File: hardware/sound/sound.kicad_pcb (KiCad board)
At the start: 2 copper layers, 177.8 x 114.3 mm, 38 parts, among them J1 Conn_01x02, J2 AVR-ISP-6, J3 Conn_01x02, J4 Conn_01x02, J5 Conn_01x02, J6 Conn_01x04, T1 125BSE, U1 6CY7, U2 SN76489, U3 ATtiny84A-P, X1 CXO_DIP8

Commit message: working on placement
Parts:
- added C10: 0.1uF, Capacitor_THT:C_Disc_D3.4mm_W2.1mm_P2.50mm, F.Cu at (101.6, 69.2)
- added C11: 2.2uF, Capacitor_THT:C_Disc_D3.4mm_W2.1mm_P2.50mm, F.Cu at (101.0, 121.9)
- added C9: 0.1uF, Capacitor_THT:C_Disc_D3.4mm_W2.1mm_P2.50mm, F.Cu at (101.6, 93.3)
- C3: value C -> 33uF 400V
- C8: value C -> 0.1uF
- LS1: footprint Connector_PinHeader_2.54mm:PinHeader_1x02_P2.54mm_Vertical -> Connector_Phoenix_MC_HighVoltage:PhoenixContact_MCV_1,5_2-G-5.08_1x02_P5.08mm_Vertical
- R10: footprint Resistor_SMD:R_1206_3216Metric_Pad1.30x1.75mm_HandSolder -> Resistor_THT:R_Axial_DIN0204_L3.6mm_D1.6mm_P5.08mm_Horizontal
- moved J5 107.2 mm to (214.0, 112.4)
- moved R10 97.5 mm to (104.8, 54.6), turned to -90 degrees
- moved J2 92.9 mm to (117.5, 54.6), turned to -90 degrees
- moved RV1 88.0 mm to (179.7, 151.3)
- moved LS1 69.3 mm to (150.5, 50.2)
- moved U3 54.8 mm to (106.0, 74.3), turned to 90 degrees
- moved R9 51.6 mm to (86.4, 126.4), turned to -90 degrees
- moved C2 49.0 mm to (212.9, 130.4), turned to 90 degrees
- moved U1 45.2 mm to (189.5, 131.2), turned to 90 degrees
- moved J3 43.2 mm to (87.6, 48.3), turned to 180 degrees
- moved R1 40.2 mm to (148.6, 151.9)
- moved C8 37.4 mm to (108.6, 123.8)
- moved D2 36.8 mm to (49.7, 99.2), turned to 90 degrees
- moved D1 35.9 mm to (49.7, 69.1), turned to -90 degrees
- moved R3 29.0 mm to (164.3, 112.8)
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
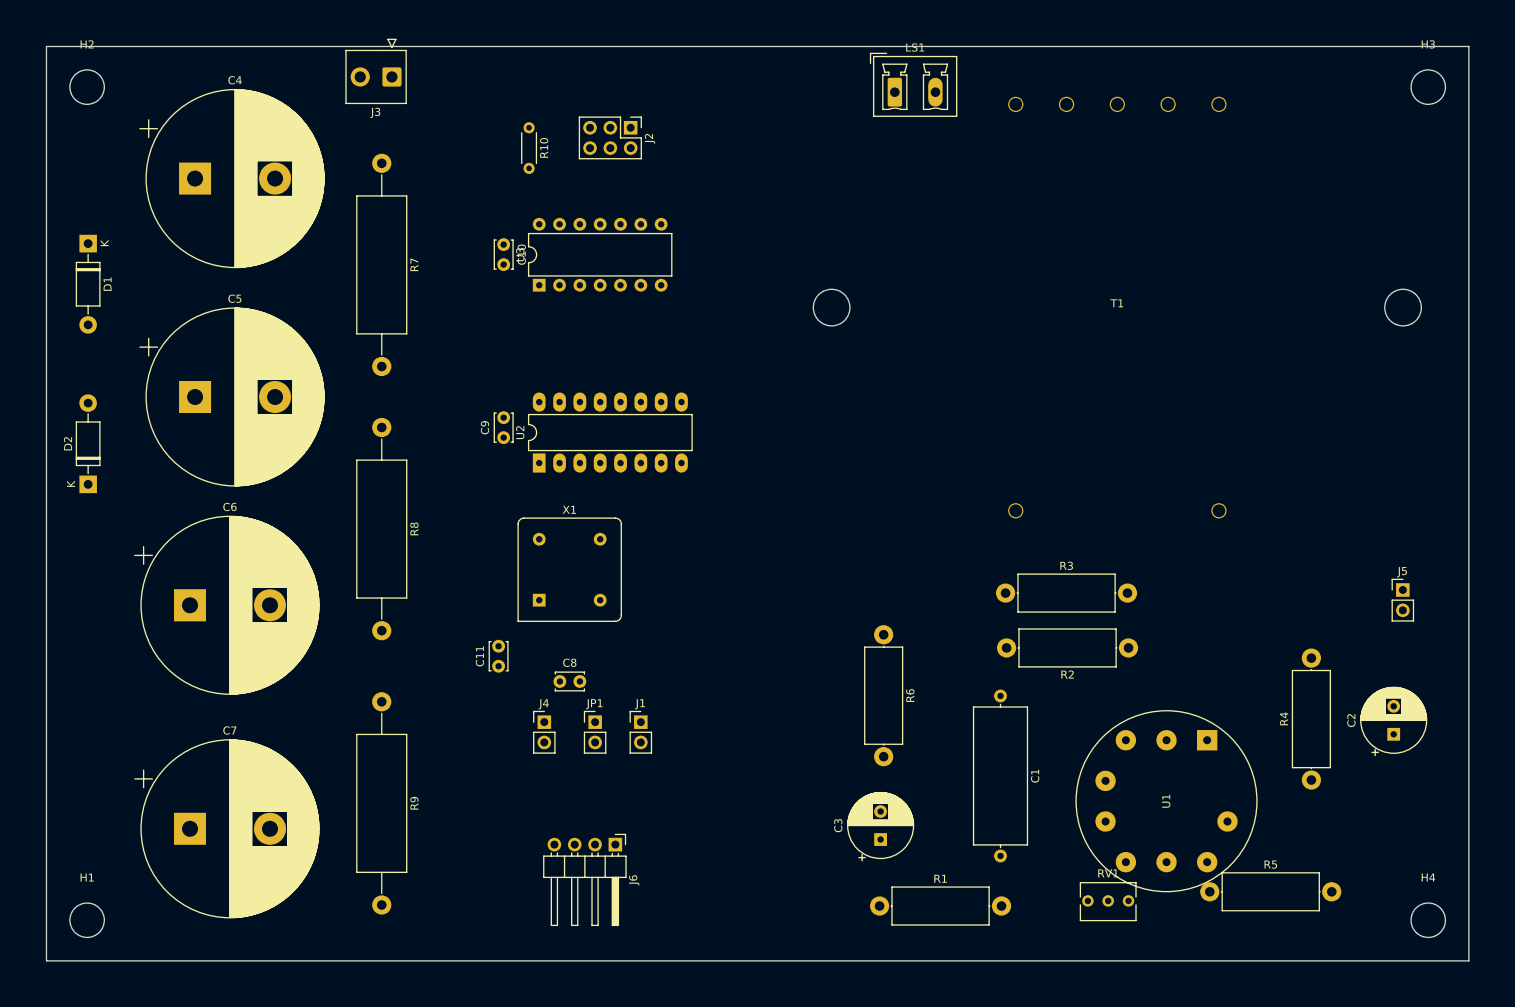
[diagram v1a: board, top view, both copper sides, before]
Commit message: work on placement, HV clearance
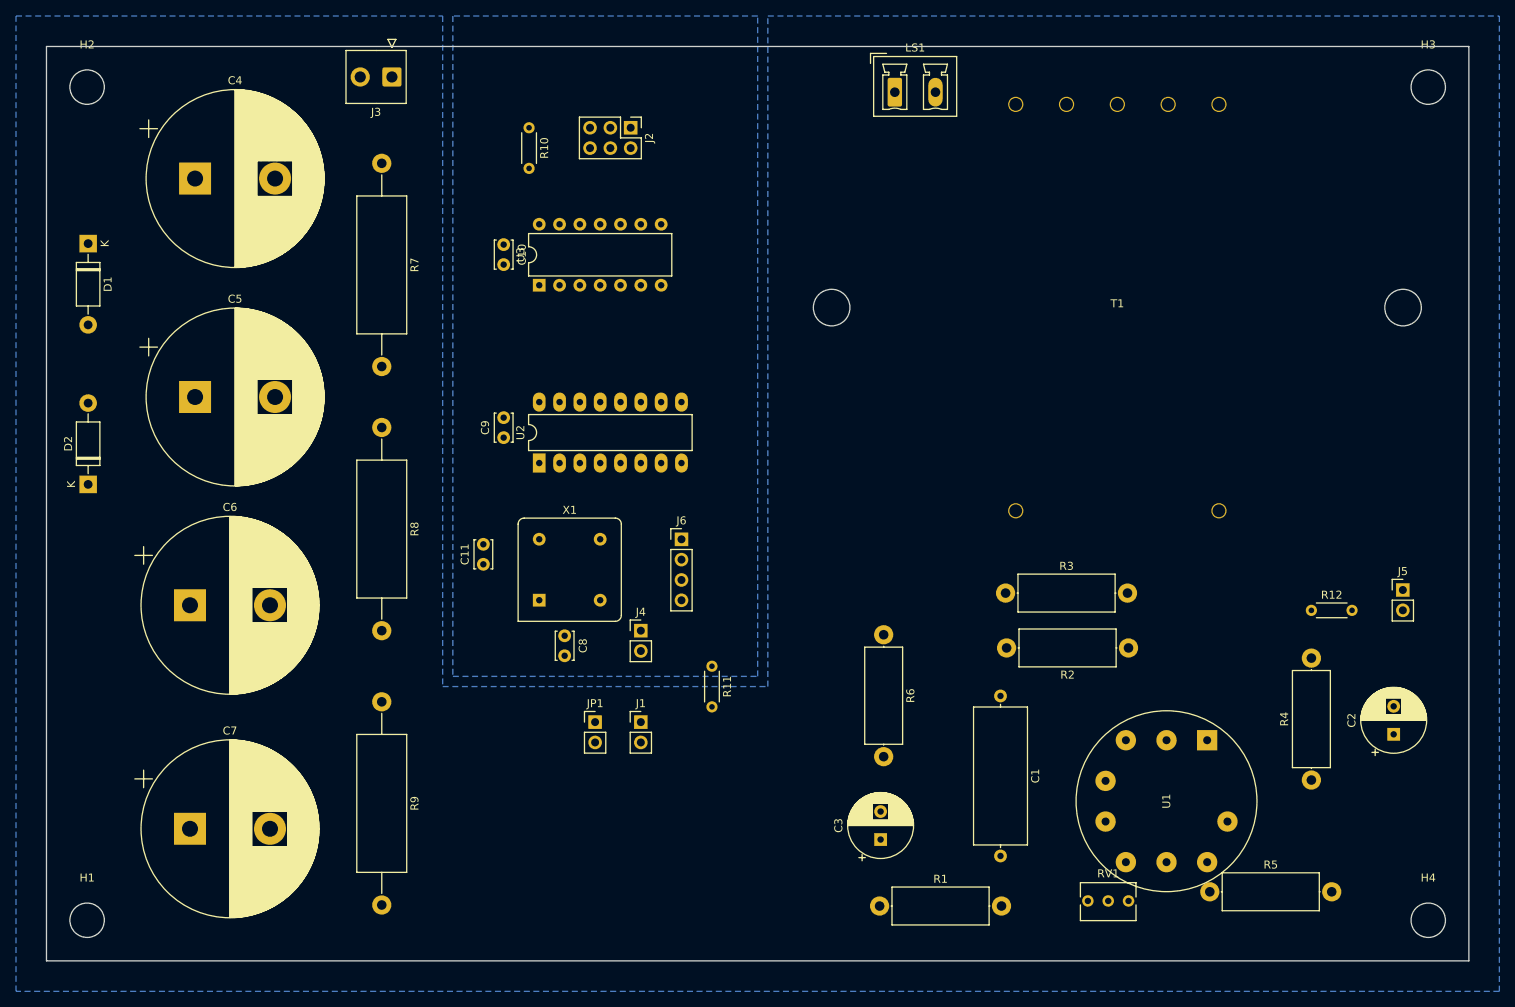
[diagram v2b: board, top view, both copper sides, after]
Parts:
- added R11: 1, Resistor_THT:R_Axial_DIN0204_L3.6mm_D1.6mm_P5.08mm_Horizontal, F.Cu at (127.6, 121.9)
- added R12: 100, Resistor_THT:R_Axial_DIN0204_L3.6mm_D1.6mm_P5.08mm_Horizontal, F.Cu at (202.6, 114.9)
- J6: footprint Connector_PinHeader_2.54mm:PinHeader_1x04_P2.54mm_Horizontal -> Connector_PinHeader_2.54mm:PinHeader_1x04_P2.54mm_Vertical
- moved J6 39.0 mm to (123.8, 106.1), turned to 0 degrees
- moved J4 16.6 mm to (118.7, 117.5)
- moved C11 12.9 mm to (99.1, 109.2)
- moved C8 5.75 mm to (109.2, 118.1), turned to -90 degrees
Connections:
- net Net-(C3-Pad1) renamed /HT_K1
- net Net-(C6-Pad1) renamed /HT_M3
- net Net-(D1-K) renamed /HT_M1
- net Net-(D2-K) renamed /HT_M2
- net Net-(J3-Pin_1) renamed /HT_IN
- net Net-(T1-BLU) renamed /HT_K2
- net Net-(U1A-A) renamed /HT_P1
- C10 pad 1: Earth -> GND
- C11 pad 1: Earth -> GND
- C9 pad 1: Earth -> GND
- J4 pad 2: Earth -> GND
- T1 pad 7: unconnected-(T1-WHT-Pad7) -> /NC1
- U2 pad 8: Earth -> GND
- U3 pad 14: Earth -> GND
- X1 pad 4: Earth -> GND
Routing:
- added copper zone on B.Cu, net Earth
- added copper zone on B.Cu, net GND
